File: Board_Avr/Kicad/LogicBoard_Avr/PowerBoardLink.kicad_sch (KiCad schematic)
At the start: 7 parts, among them J4 Conn_01x08

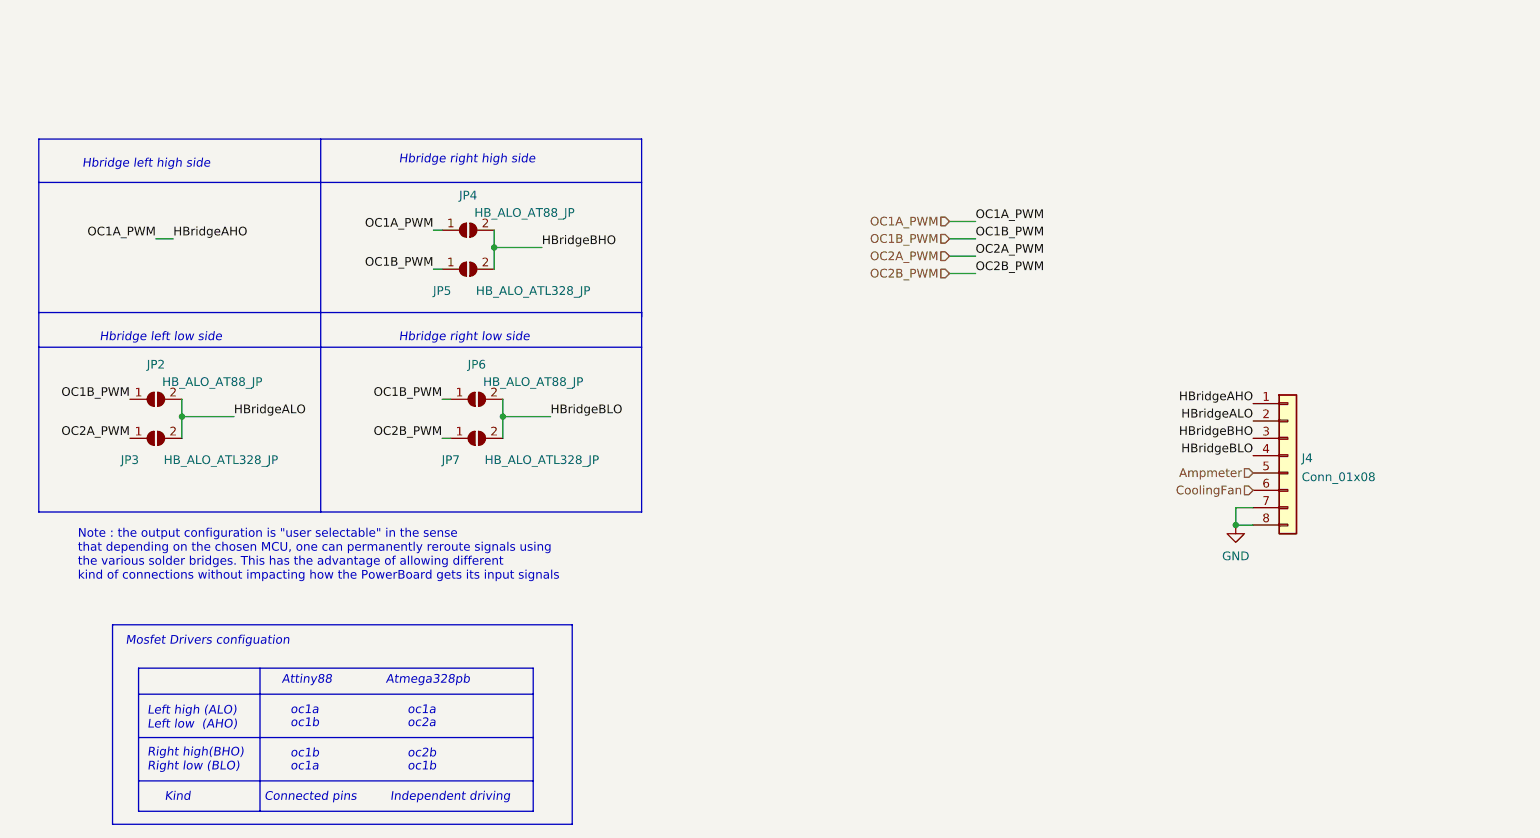
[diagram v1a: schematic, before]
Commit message: Fixed misorganised pins and updated pin mapping table
Signed-off-by: bebenlebricolo <benoittarrade@hotmail.fr>
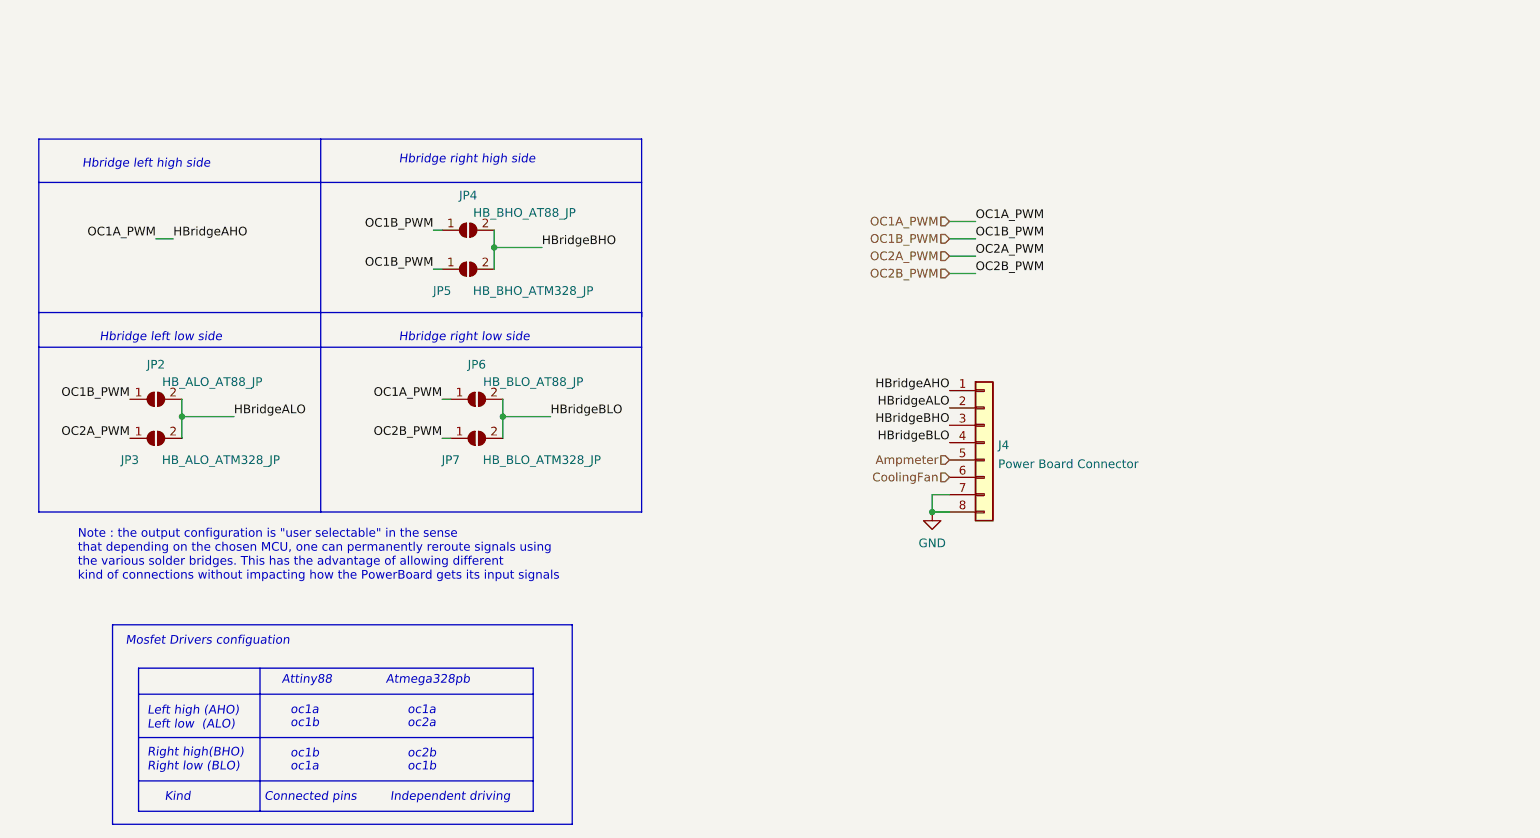
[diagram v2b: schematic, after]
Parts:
- J4: value Conn_01x08 -> Power Board Connector
- JP3: value HB_ALO_ATL328_JP -> HB_ALO_ATM328_JP
- JP4: value HB_ALO_AT88_JP -> HB_BHO_AT88_JP
- JP5: value HB_ALO_ATL328_JP -> HB_BHO_ATM328_JP
- JP6: value HB_ALO_AT88_JP -> HB_BLO_AT88_JP
- JP7: value HB_ALO_ATL328_JP -> HB_BLO_ATM328_JP
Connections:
- net OC1A_PWM: now also JP6.1 (A); no longer JP4.1 (A)
- net OC1B_PWM: now also JP4.1 (A); no longer JP6.1 (A)
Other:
- note added: "Left high (AHO) Left low (ALO) Right high(BHO) Right low (BLO)"
- note removed: "Left high (ALO) Left low (AHO) Right high(BHO) Right low (BLO)"
- moved on the sheet: J4
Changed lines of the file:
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@@
   (junction (at 98.425 48.895) (diameter 0) (color 0 0 0 0)
   )
-  (junction (at 207.01 89.535) (diameter 0) (color 0 0 0 0)
+  (junction (at 162.56 87.63) (diameter 0) (color 0 0 0 0)
   )
   (junction (at 52.705 73.66) (diameter 0) (color 0 0 0 0)
@@
     (stroke (width 0) (type default) (color 0 0 0 0))
   )
-  (wire (pts (xy 207.01 89.535) (xy 209.55 89.535))
+  (wire (pts (xy 162.56 87.63) (xy 165.1 87.63))
     (stroke (width 0) (type default) (color 0 0 0 0))
   )
@@
     (stroke (width 0) (type default) (color 0 0 0 0))
   )
-  (wire (pts (xy 207.01 86.995) (xy 207.01 89.535))
+  (wire (pts (xy 162.56 85.09) (xy 162.56 87.63))
     (stroke (width 0) (type default) (color 0 0 0 0))
   )
@@
     (stroke (width 0) (type default) (color 0 0 0 0))
   )
-  (wire (pts (xy 209.55 86.995) (xy 207.01 86.995))
+  (wire (pts (xy 165.1 85.09) (xy 162.56 85.09))
     (stroke (width 0) (type default) (color 0 0 0 0))
   )
@@
     (effects (font (size 1.27 1.27) italic) (justify left bottom))
   )
-  (text "Left high (ALO)\nLeft low  (AHO)\n\nRight high(BHO)	\nRight low (BLO)"
+  (text "Left high (AHO)\nLeft low  (ALO)\n\nRight high(BHO)	\nRight low (BLO)"
     (at 47.625 125.73 0)
     (effects (font (size 1.27 1.27) italic) (justify left bottom))
@@
     (effects (font (size 1.27 1.27) italic) (justify left bottom))
   )
-  (label "OC1A_PWM" (at 89.535 46.355 180)
-    (effects (font (size 1.27 1.27)) (justify right bottom))
-  )
   (label "HBridgeAHO" (at 51.435 47.625 0)
     (effects (font (size 1.27 1.27)) (justify left bottom))
   )
-  (label "HBridgeALO" (at 209.55 74.295 180)
+  (label "HBridgeALO" (at 165.1 72.39 180)
     (effects (font (size 1.27 1.27)) (justify right bottom))
   )
@@
     (effects (font (size 1.27 1.27)) (justify left bottom))
   )
-  (label "HBridgeAHO" (at 209.55 71.755 180)
+  (label "HBridgeAHO" (at 165.1 69.85 180)
     (effects (font (size 1.27 1.27)) (justify right bottom))
   )
@@
     (effects (font (size 1.27 1.27)) (justify left bottom))
   )
+  (label "OC1A_PWM" (at 90.805 71.12 180)
+    (effects (font (size 1.27 1.27)) (justify right bottom))
+  )
   (label "OC1A_PWM" (at 168.91 45.085 0)
     (effects (font (size 1.27 1.27)) (justify left bottom))
@@
     (effects (font (size 1.27 1.27)) (justify right bottom))
   )
-  (label "OC1B_PWM" (at 90.805 71.12 180)
+  (label "OC1B_PWM" (at 89.535 46.355 180)
     (effects (font (size 1.27 1.27)) (justify right bottom))
   )
@@
     (effects (font (size 1.27 1.27)) (justify right bottom))
   )
-  (label "HBridgeBLO" (at 209.55 79.375 180)
-    (effects (font (size 1.27 1.27)) (justify right bottom))
-  )
-  (label "HBridgeBHO" (at 209.55 76.835 180)
+  (label "HBridgeBLO" (at 165.1 77.47 180)
+    (effects (font (size 1.27 1.27)) (justify right bottom))
+  )
+  (label "HBridgeBHO" (at 165.1 74.93 180)
     (effects (font (size 1.27 1.27)) (justify right bottom))
   )
@@
     (effects (font (size 1.27 1.27)) (justify right))
   )
-  (hierarchical_label "Ampmeter" (shape input) (at 209.55 81.915 180)
+  (hierarchical_label "Ampmeter" (shape input) (at 165.1 80.01 180)
     (effects (font (size 1.27 1.27)) (justify right))
   )
@@
     (effects (font (size 1.27 1.27)) (justify right))
   )
-  (hierarchical_label "CoolingFan" (shape input) (at 209.55 84.455 180)
+  (hierarchical_label "CoolingFan" (shape input) (at 165.1 82.55 180)
     (effects (font (size 1.27 1.27)) (justify right))
   )
@@
     (in_bom yes) (on_board yes)
     (property "Reference" "JP6" (id 0) (at 95.885 66.04 0))
-    (property "Value" "HB_ALO_AT88_JP" (id 1) (at 104.14 68.58 0))
+    (property "Value" "HB_BLO_AT88_JP" (id 1) (at 104.14 68.58 0))
     (property "Footprint" "" (id 2) (at 95.885 71.12 0)
       (effects (font (size 1.27 1.27)) hide)
@@
     (in_bom yes) (on_board yes)
     (property "Reference" "JP7" (id 0) (at 92.075 80.01 0))
-    (property "Value" "HB_ALO_ATL328_JP" (id 1) (at 105.41 80.01 0))
+    (property "Value" "HB_BLO_ATM328_JP" (id 1) (at 105.41 80.01 0))
     (property "Footprint" "" (id 2) (at 95.885 76.835 0)
       (effects (font (size 1.27 1.27)) hide)
@@
     (in_bom yes) (on_board yes)
     (property "Reference" "JP4" (id 0) (at 94.615 41.275 0))
-    (property "Value" "HB_ALO_AT88_JP" (id 1) (at 102.87 43.815 0))
+    (property "Value" "HB_BHO_AT88_JP" (id 1) (at 102.87 43.815 0))
     (property "Footprint" "" (id 2) (at 94.615 46.355 0)
       (effects (font (size 1.27 1.27)) hide)
@@
     (pin "2")
   )
-  (symbol (lib_id "Connector_Generic:Conn_01x08") (at 214.63 79.375 0) (unit 1)
+  (symbol (lib_id "Connector_Generic:Conn_01x08") (at 170.18 77.47 0) (unit 1)
     (in_bom yes) (on_board yes) (fields_autoplaced)
-    (property "Reference" "J4" (id 0) (at 216.662 79.7365 0)
+    (property "Reference" "J4" (id 0) (at 172.212 77.8315 0)
       (effects (font (size 1.27 1.27)) (justify left))
     )
-    (property "Value" "Conn_01x08" (id 1) (at 216.662 82.5116 0)
+    (property "Value" "Power Board Connector" (id 1) (at 172.212 80.6066 0)
       (effects (font (size 1.27 1.27)) (justify left))
     )
-    (property "Footprint" "" (id 2) (at 214.63 79.375 0)
-      (effects (font (size 1.27 1.27)) hide)
-    )
-    (property "Datasheet" "~" (id 3) (at 214.63 79.375 0)
+    (property "Footprint" "" (id 2) (at 170.18 77.47 0)
+      (effects (font (size 1.27 1.27)) hide)
+    )
+    (property "Datasheet" "~" (id 3) (at 170.18 77.47 0)
       (effects (font (size 1.27 1.27)) hide)
     )
@@
     (in_bom yes) (on_board yes)
     (property "Reference" "JP5" (id 0) (at 90.805 55.245 0))
-    (property "Value" "HB_ALO_ATL328_JP" (id 1) (at 104.14 55.245 0))
+    (property "Value" "HB_BHO_ATM328_JP" (id 1) (at 104.14 55.245 0))
     (property "Footprint" "" (id 2) (at 94.615 52.07 0)
       (effects (font (size 1.27 1.27)) hide)
@@
     (in_bom yes) (on_board yes)
     (property "Reference" "JP3" (id 0) (at 45.085 80.01 0))
-    (property "Value" "HB_ALO_ATL328_JP" (id 1) (at 58.42 80.01 0))
+    (property "Value" "HB_ALO_ATM328_JP" (id 1) (at 58.42 80.01 0))
     (property "Footprint" "" (id 2) (at 48.895 76.835 0)
       (effects (font (size 1.27 1.27)) hide)
@@
     (pin "2")
   )
-  (symbol (lib_id "power:GND") (at 207.01 89.535 0) (unit 1)
+  (symbol (lib_id "power:GND") (at 162.56 87.63 0) (unit 1)
     (in_bom yes) (on_board yes) (fields_autoplaced)
-    (property "Reference" "#PWR0130" (id 0) (at 207.01 95.885 0)
-      (effects (font (size 1.27 1.27)) hide)
-    )
-    (property "Value" "GND" (id 1) (at 207.01 94.0975 0))
-    (property "Footprint" "" (id 2) (at 207.01 89.535 0)
-      (effects (font (size 1.27 1.27)) hide)
-    )
-    (property "Datasheet" "" (id 3) (at 207.01 89.535 0)
-      (effects (font (size 1.27 1.27)) hide)
-    )
+    (property "Reference" "#PWR0130" (id 0) (at 162.56 93.98 0)
+      (effects (font (size 1.27 1.27)) hide)
+    )
+    (property "Value" "GND" (id 1) (at 162.56 92.1925 0))
+    (property "Footprint" "" (id 2) (at 162.56 87.63 0)
+      (effects (font (size 1.27 1.27)) hide)
+    )
+    (property "Datasheet" "" (id 3) (at 162.56 87.63 0)
+      (effects (font (size 1.27 1.27)) hide)
+    )
